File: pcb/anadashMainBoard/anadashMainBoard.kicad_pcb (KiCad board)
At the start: 2 copper layers, 17 parts, among them J1 DisplayConnector, J2 LeftKeyConnector, J3 RightKeyConnector, J4 EncoderConnector

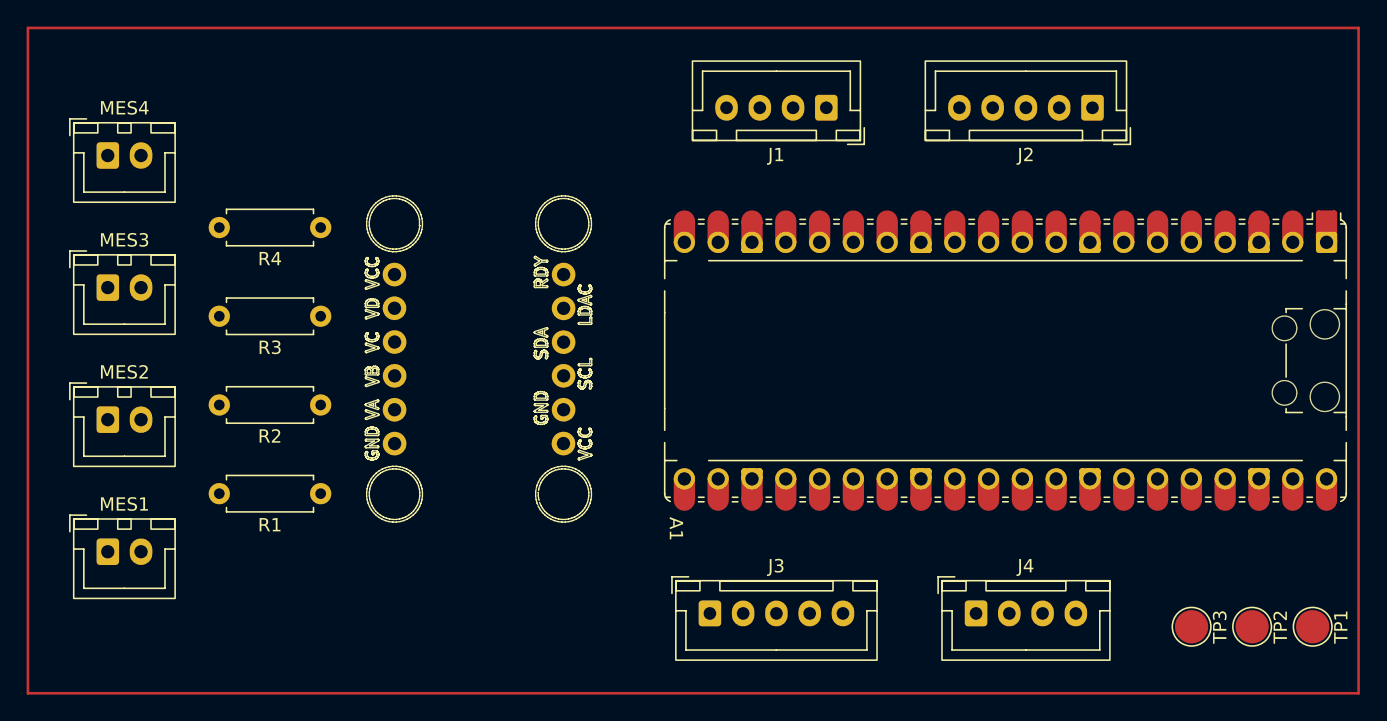
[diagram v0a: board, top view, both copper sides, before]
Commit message: Made the mainboard PCB
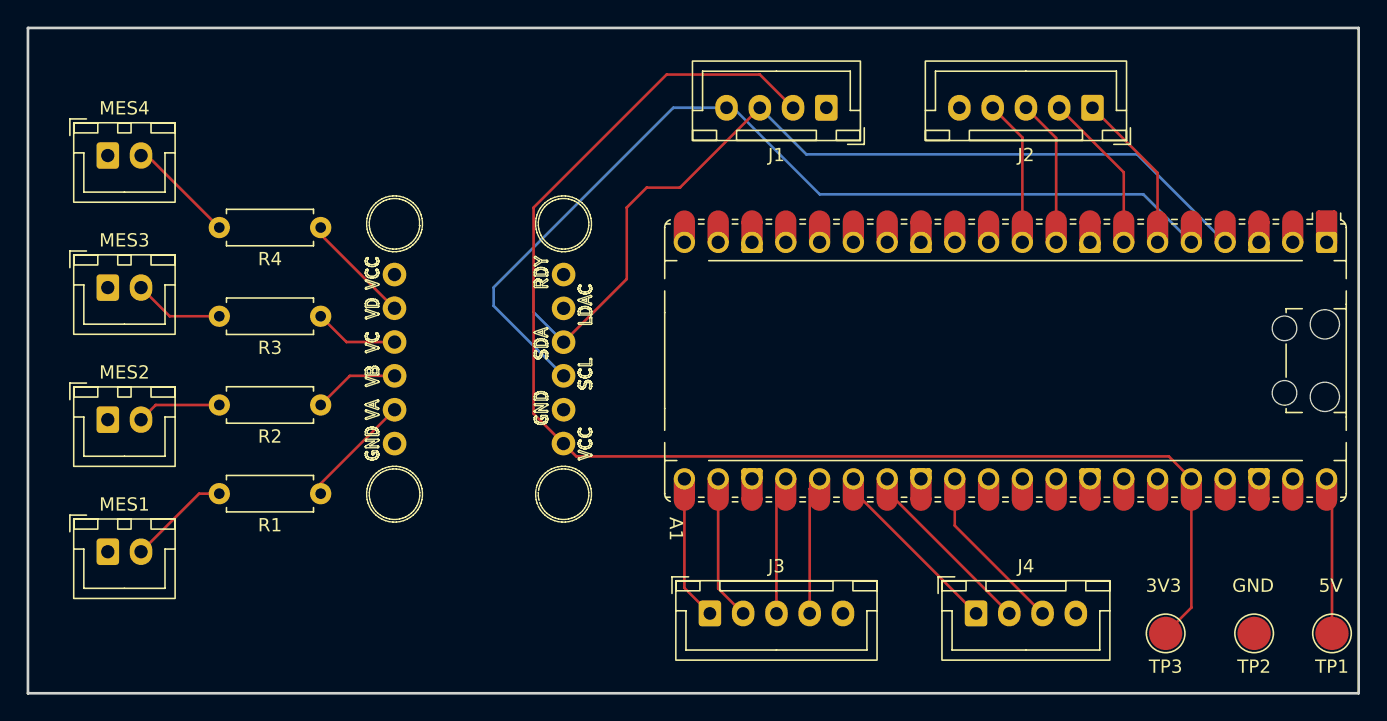
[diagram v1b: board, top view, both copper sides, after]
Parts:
- moved TP3 2.01 mm to (193.5, 115.5), turned to 180 degrees
- moved TP1 1.53 mm to (206.0, 115.5), turned to 180 degrees
- moved TP2 0.52 mm to (200.1, 115.5), turned to 180 degrees
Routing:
- net +3V3: track 0.00 -> 104.4 mm
- net SCL: track 0.00 -> 71.0 mm
- net SDA: track 0.00 -> 69.9 mm
- net Net-(A1-GPIO21): track 0.00 -> 14.0 mm
- net Net-(A1-GPIO20): track 0.00 -> 14.0 mm
- net Net-(A1-GPIO22): track 0.00 -> 12.8 mm
- net Net-(A1-GPIO4): track 0.00 -> 12.1 mm
- net Net-(A1-GPIO5): track 0.00 -> 12.1 mm
- net +5V: track 0.00 -> 11.8 mm
- net Net-(A1-GPIO6): track 0.00 -> 11.1 mm
- net Net-(A1-GPIO7): track 0.00 -> 11.0 mm
- net Net-(A1-GPIO16): track 0.00 -> 10.9 mm
- net Net-(A1-GPIO17): track 0.00 -> 10.9 mm
- net Net-(A1-GPIO19): track 0.00 -> 10.4 mm
- net Net-(A1-GPIO18): track 0.00 -> 10.4 mm
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- added copper zone on B.Cu, net GND
- added copper zone on F.Cu, net GND
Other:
- board outline added: 100 x 50 mm
- board text added: "3V3"
- board text added: "5V"
- board text added: "GND"

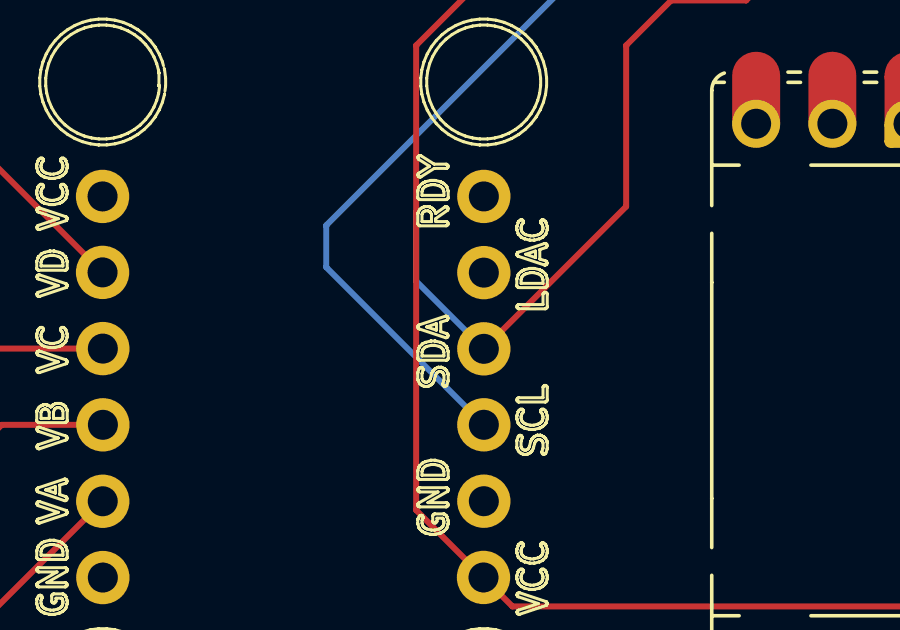
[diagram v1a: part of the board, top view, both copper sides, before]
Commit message: Improve the mainboard pcb's 3d model
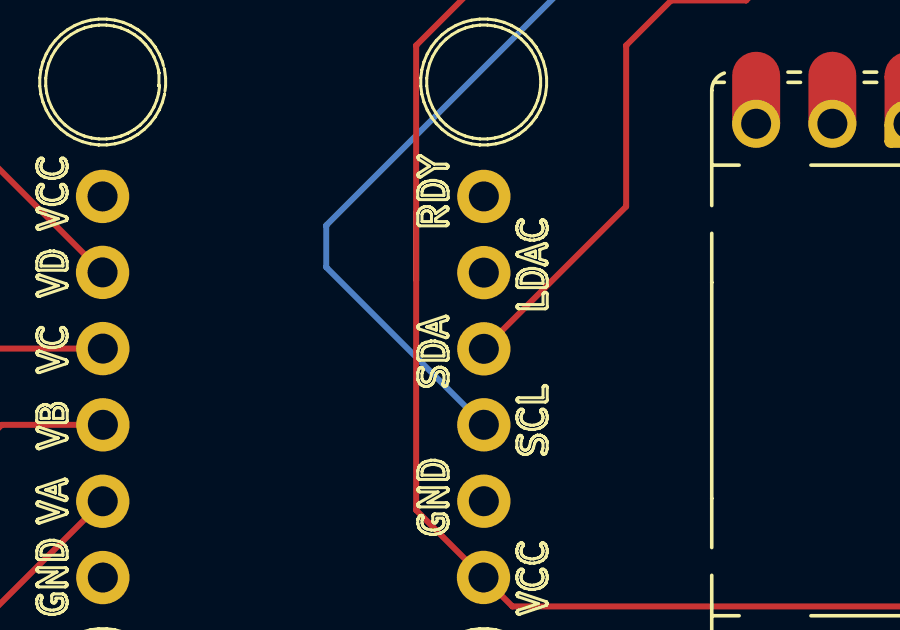
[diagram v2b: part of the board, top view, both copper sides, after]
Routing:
- net SDA: track 69.9 -> 66.7 mm
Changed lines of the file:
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@@
 		(model "../3dshapes/Adafruit_MCP4728.STEP"
 			(offset
-				(xyz 50 8.875 0)
+				(xyz -0.7 -21 0)
 			)
 			(scale
@@
 		(width 0.2)
 		(layer "B.Cu")
-		(net "SDA")
-	)
-	(segment
-		(start 148.255699 93.613126)
-		(end 146 91.357427)
-		(width 0.2)
-		(layer "B.Cu")
